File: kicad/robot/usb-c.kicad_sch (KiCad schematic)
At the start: 11 parts

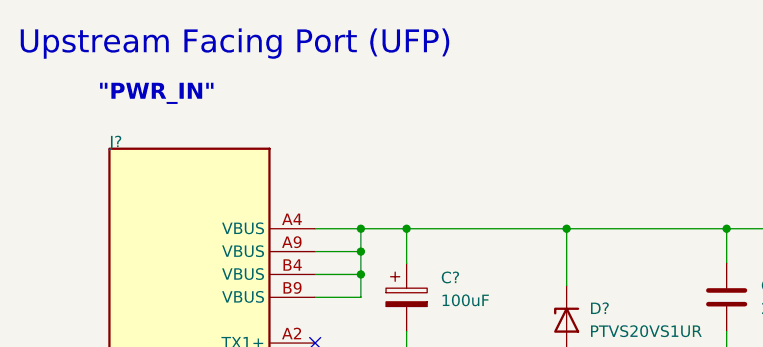
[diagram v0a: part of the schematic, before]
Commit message: Removed some outdated text
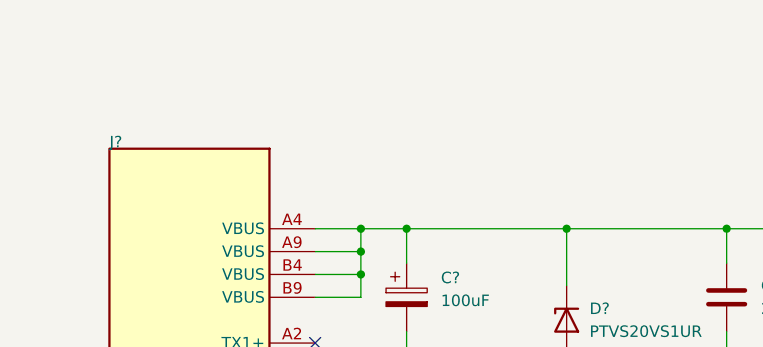
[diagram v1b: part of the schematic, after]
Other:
- note removed: ""PWR_IN""
- note removed: "Upstream Facing Port (UFP)"
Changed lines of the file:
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@@
     (stroke (width 0.254) (type default) (color 0 0 0 0))
-  )
-  (text "\"PWR_IN\"" (at 115.57 57.15 180)
-    (effects (font (size 1.778 1.778) bold) (justify left bottom))
-  )
-  (text "Upstream Facing Port (UFP)" (at 106.68 52.07 180)
-    (effects (font (size 2.54 2.54)) (justify left bottom))
   )
   (label "D-" (at 139.7 116.84 0)

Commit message: Automated annotation for full project
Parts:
- gave numbers to parts that had none: 11
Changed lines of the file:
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@@
   (symbol (lib_id "Device:C") (at 185.42 78.74 0) (unit 1)
     (in_bom yes) (on_board yes) (fields_autoplaced)
-    (property "Reference" "C?" (id 0) (at 189.23 77.4699 0)
+    (property "Reference" "C20" (id 0) (at 189.23 77.4699 0)
       (effects (font (size 1.27 1.27)) (justify left))
     )
@@
   (symbol (lib_id "Connector:TestPoint") (at 157.48 124.46 270) (unit 1)
     (in_bom yes) (on_board yes)
-    (property "Reference" "TP?" (id 0) (at 162.56 121.92 90)
+    (property "Reference" "TP8" (id 0) (at 162.56 121.92 90)
       (effects (font (size 1.27 1.27)) (justify left))
     )
@@
   (symbol (lib_id "Device:D_Zener") (at 167.64 81.28 90) (mirror x) (unit 1)
     (in_bom yes) (on_board yes)
-    (property "Reference" "D?" (id 0) (at 170.18 80.0099 90)
+    (property "Reference" "D2" (id 0) (at 170.18 80.0099 90)
       (effects (font (size 1.27 1.27)) (justify right))
     )
@@
   (symbol (lib_id "Device:C_Polarized") (at 149.86 78.74 0) (unit 1)
     (in_bom yes) (on_board yes) (fields_autoplaced)
-    (property "Reference" "C?" (id 0) (at 153.67 76.5809 0)
+    (property "Reference" "C4" (id 0) (at 153.67 76.5809 0)
       (effects (font (size 1.27 1.27)) (justify left))
     )
@@
   (symbol (lib_id "Connector:TestPoint") (at 175.26 129.54 0) (unit 1)
     (in_bom yes) (on_board yes)
-    (property "Reference" "TP?" (id 0) (at 177.8 124.46 0)
+    (property "Reference" "TP9" (id 0) (at 177.8 124.46 0)
       (effects (font (size 1.27 1.27)) (justify left))
     )
@@
   (symbol (lib_id "Device:C") (at 170.18 142.24 0) (unit 1)
     (in_bom yes) (on_board yes) (fields_autoplaced)
-    (property "Reference" "C?" (id 0) (at 173.99 140.9699 0)
+    (property "Reference" "C19" (id 0) (at 173.99 140.9699 0)
       (effects (font (size 1.27 1.27)) (justify left))
     )
@@
   (symbol (lib_id "Connector:TestPoint") (at 193.04 71.12 0) (unit 1)
     (in_bom yes) (on_board yes)
-    (property "Reference" "TP?" (id 0) (at 195.58 66.04 0)
+    (property "Reference" "TP11" (id 0) (at 195.58 66.04 0)
       (effects (font (size 1.27 1.27)) (justify left))
     )
@@
   (symbol (lib_id "Top-altium-import:0_mirrored_USBC_Receptacle_SMD_RA") (at 134.62 62.23 0) (unit 1)
     (in_bom yes) (on_board yes)
-    (property "Reference" "J?" (id 0) (at 116.84 62.23 0)
+    (property "Reference" "J1" (id 0) (at 116.84 62.23 0)
       (effects (font (size 1.27 1.27)) (justify left bottom))
     )
@@
   (symbol (lib_id "Connector:TestPoint") (at 147.32 121.92 270) (unit 1)
     (in_bom yes) (on_board yes) (fields_autoplaced)
-    (property "Reference" "TP?" (id 0) (at 152.4 120.6499 90)
+    (property "Reference" "TP7" (id 0) (at 152.4 120.6499 90)
       (effects (font (size 1.27 1.27)) (justify left))
     )
@@
   (symbol (lib_id "Connector:TestPoint") (at 175.26 132.08 180) (unit 1)
     (in_bom yes) (on_board yes)
-    (property "Reference" "TP?" (id 0) (at 177.8 134.62 0)
+    (property "Reference" "TP10" (id 0) (at 177.8 134.62 0)
       (effects (font (size 1.27 1.27)) (justify right))
     )
@@
   (symbol (lib_id "Device:C") (at 157.48 142.24 0) (unit 1)
     (in_bom yes) (on_board yes)
-    (property "Reference" "C?" (id 0) (at 160.782 140.97 0)
-      (effects (font (size 1.27 1.27)) (justify left))
-    )
+    (property "Reference" "C18" (id 0) (at 160.782 140.97 0)
+      (effects (font (size 1.27 1.27)) (justify left))
+    )

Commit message: Moved USB-C symbol to connector lib
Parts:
- J1: symbol Top-altium-import:0_mirrored_USBC_Receptacle_SMD_RA -> Connector:0_mirrored_USBC_Receptacle_SMD_RA
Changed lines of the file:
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@@
     (pin "1")
   )
-  (symbol (lib_id "Top-altium-import:0_mirrored_USBC_Receptacle_SMD_RA") (at 134.62 62.23 0) (unit 1)
+  (symbol (lib_id "Connector:0_mirrored_USBC_Receptacle_SMD_RA") (at 134.62 62.23 0) (unit 1)
     (in_bom yes) (on_board yes)
     (property "Reference" "J1" (id 0) (at 116.84 62.23 0)

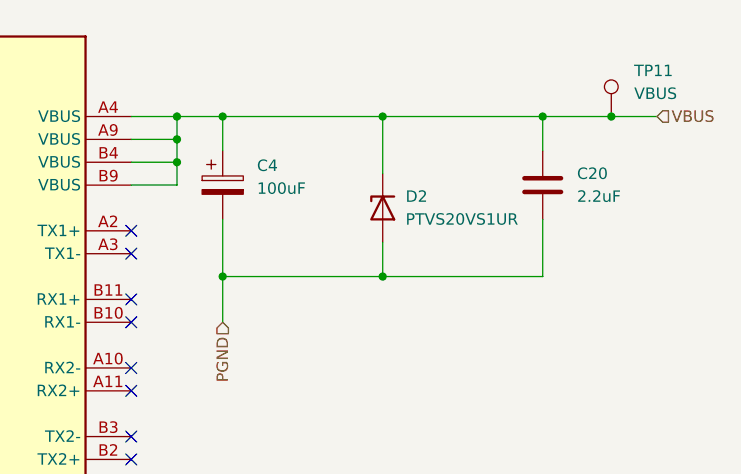
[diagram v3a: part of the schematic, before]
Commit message: Assigned capacitor footprints
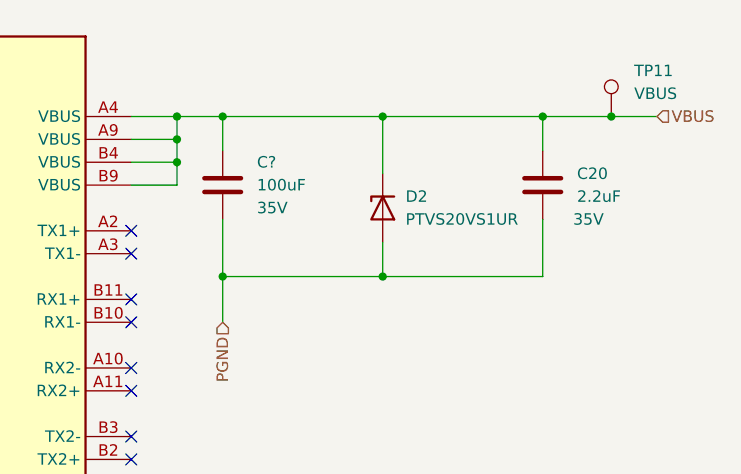
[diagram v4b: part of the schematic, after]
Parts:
- removed C4: 100uF, symbol Device:C_Polarized
- added C?: 100uF, Capacitor_SMD:C_1210_3225Metric, symbol Device:C
- C18, C19: footprint (none) -> Capacitor_SMD:C_0402_1005Metric
- C20: footprint (none) -> Capacitor_SMD:C_0805_2012Metric
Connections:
- net PGND: now also C?.2
- net VBUS: now also C?.1
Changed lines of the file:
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@@
   )
   (symbol (lib_id "Device:C") (at 185.42 78.74 0) (unit 1)
+    (in_bom yes) (on_board yes)
+    (property "Reference" "C20" (id 0) (at 189.23 77.4699 0)
+      (effects (font (size 1.27 1.27)) (justify left))
+    )
+    (property "Value" "2.2uF" (id 1) (at 189.23 80.0099 0)
+      (effects (font (size 1.27 1.27)) (justify left))
+    )
+    (property "Footprint" "Capacitor_SMD:C_0805_2012Metric" (id 2) (at 186.3852 82.55 0)
+      (effects (font (size 1.27 1.27)) hide)
+    )
+    (property "Datasheet" "~" (id 3) (at 185.42 78.74 0)
+      (effects (font (size 1.27 1.27)) hide)
+    )
+    (property "Description" "35V" (id 4) (at 190.5 82.55 0))
+    (pin "1")
+    (pin "2")
+  )
+  (symbol (lib_id "Connector:TestPoint") (at 157.48 124.46 270) (unit 1)
+    (in_bom yes) (on_board yes)
+    (property "Reference" "TP8" (id 0) (at 162.56 121.92 90)
+      (effects (font (size 1.27 1.27)) (justify left))
+    )
+    (property "Value" "D+" (id 1) (at 162.56 124.46 90)
+      (effects (font (size 1.27 1.27)) (justify left))
+    )
+    (property "Footprint" "" (id 2) (at 157.48 129.54 0)
+      (effects (font (size 1.27 1.27)) hide)
+    )
+    (property "Datasheet" "~" (id 3) (at 157.48 129.54 0)
+      (effects (font (size 1.27 1.27)) hide)
+    )
+    (pin "1")
+  )
+  (symbol (lib_id "Device:D_Zener") (at 167.64 81.28 90) (mirror x) (unit 1)
+    (in_bom yes) (on_board yes)
+    (property "Reference" "D2" (id 0) (at 170.18 80.0099 90)
+      (effects (font (size 1.27 1.27)) (justify right))
+    )
+    (property "Value" "PTVS20VS1UR" (id 1) (at 170.18 82.5499 90)
+      (effects (font (size 1.27 1.27)) (justify right))
+    )
+    (property "Footprint" "" (id 2) (at 167.64 81.28 0)
+      (effects (font (size 1.27 1.27)) hide)
+    )
+    (property "Datasheet" "~" (id 3) (at 167.64 81.28 0)
+      (effects (font (size 1.27 1.27)) hide)
+    )
+    (pin "1")
+    (pin "2")
+  )
+  (symbol (lib_id "Device:C") (at 149.86 78.74 0) (unit 1)
     (in_bom yes) (on_board yes) (fields_autoplaced)
-    (property "Reference" "C20" (id 0) (at 189.23 77.4699 0)
-      (effects (font (size 1.27 1.27)) (justify left))
-    )
-    (property "Value" "2.2uF" (id 1) (at 189.23 80.0099 0)
-      (effects (font (size 1.27 1.27)) (justify left))
-    )
-    (property "Footprint" "" (id 2) (at 186.3852 82.55 0)
-      (effects (font (size 1.27 1.27)) hide)
-    )
-    (property "Datasheet" "~" (id 3) (at 185.42 78.74 0)
-      (effects (font (size 1.27 1.27)) hide)
-    )
-    (pin "1")
-    (pin "2")
-  )
-  (symbol (lib_id "Connector:TestPoint") (at 157.48 124.46 270) (unit 1)
-    (in_bom yes) (on_board yes)
-    (property "Reference" "TP8" (id 0) (at 162.56 121.92 90)
-      (effects (font (size 1.27 1.27)) (justify left))
-    )
-    (property "Value" "D+" (id 1) (at 162.56 124.46 90)
-      (effects (font (size 1.27 1.27)) (justify left))
-    )
-    (property "Footprint" "" (id 2) (at 157.48 129.54 0)
-      (effects (font (size 1.27 1.27)) hide)
-    )
-    (property "Datasheet" "~" (id 3) (at 157.48 129.54 0)
-      (effects (font (size 1.27 1.27)) hide)
-    )
-    (pin "1")
-  )
-  (symbol (lib_id "Device:D_Zener") (at 167.64 81.28 90) (mirror x) (unit 1)
-    (in_bom yes) (on_board yes)
-    (property "Reference" "D2" (id 0) (at 170.18 80.0099 90)
-      (effects (font (size 1.27 1.27)) (justify right))
-    )
-    (property "Value" "PTVS20VS1UR" (id 1) (at 170.18 82.5499 90)
-      (effects (font (size 1.27 1.27)) (justify right))
-    )
-    (property "Footprint" "" (id 2) (at 167.64 81.28 0)
-      (effects (font (size 1.27 1.27)) hide)
-    )
-    (property "Datasheet" "~" (id 3) (at 167.64 81.28 0)
-      (effects (font (size 1.27 1.27)) hide)
-    )
-    (pin "1")
-    (pin "2")
-  )
-  (symbol (lib_id "Device:C_Polarized") (at 149.86 78.74 0) (unit 1)
-    (in_bom yes) (on_board yes) (fields_autoplaced)
-    (property "Reference" "C4" (id 0) (at 153.67 76.5809 0)
-      (effects (font (size 1.27 1.27)) (justify left))
-    )
-    (property "Value" "100uF" (id 1) (at 153.67 79.1209 0)
-      (effects (font (size 1.27 1.27)) (justify left))
-    )
-    (property "Footprint" "" (id 2) (at 150.8252 82.55 0)
+    (property "Reference" "C?" (id 0) (at 153.67 76.1999 0)
+      (effects (font (size 1.27 1.27)) (justify left))
+    )
+    (property "Value" "100uF" (id 1) (at 153.67 78.7399 0)
+      (effects (font (size 1.27 1.27)) (justify left))
+    )
+    (property "Footprint" "Capacitor_SMD:C_1210_3225Metric" (id 2) (at 150.8252 82.55 0)
       (effects (font (size 1.27 1.27)) hide)
     )
     (property "Datasheet" "~" (id 3) (at 149.86 78.74 0)
       (effects (font (size 1.27 1.27)) hide)
+    )
+    (property "Description" "35V" (id 4) (at 153.67 81.2799 0)
+      (effects (font (size 1.27 1.27)) (justify left))
     )
     (pin "1")
@@
       (effects (font (size 1.27 1.27)) (justify left))
     )
-    (property "Footprint" "" (id 2) (at 171.1452 146.05 0)
+    (property "Footprint" "Capacitor_SMD:C_0402_1005Metric" (id 2) (at 171.1452 146.05 0)
       (effects (font (size 1.27 1.27)) hide)
     )
@@
       (effects (font (size 1.27 1.27)) (justify left))
     )
-    (property "Footprint" "" (id 2) (at 158.4452 146.05 0)
-      (effects (font (size 1.27 1.27)) hide)
-    )
+    (property "Footprint" "Capacitor_SMD:C_0402_1005Metric" (id 2) (at 158.4452 146.05 0)
+      (effects (font (size 1.27 1.27)) hide)
+    )

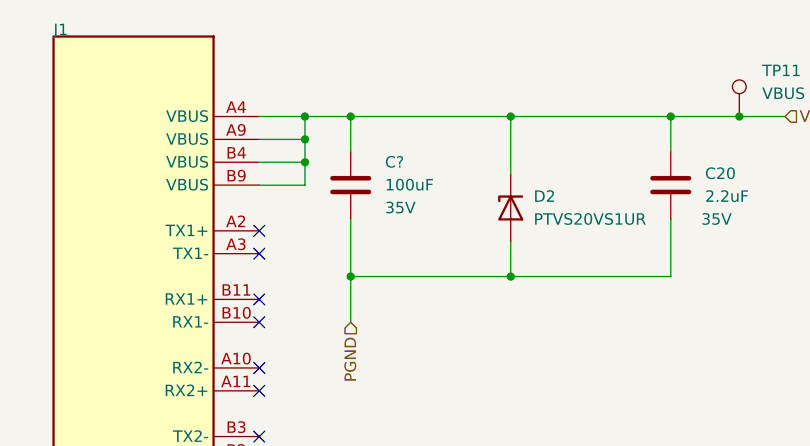
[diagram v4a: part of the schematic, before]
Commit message: Added missing annotations
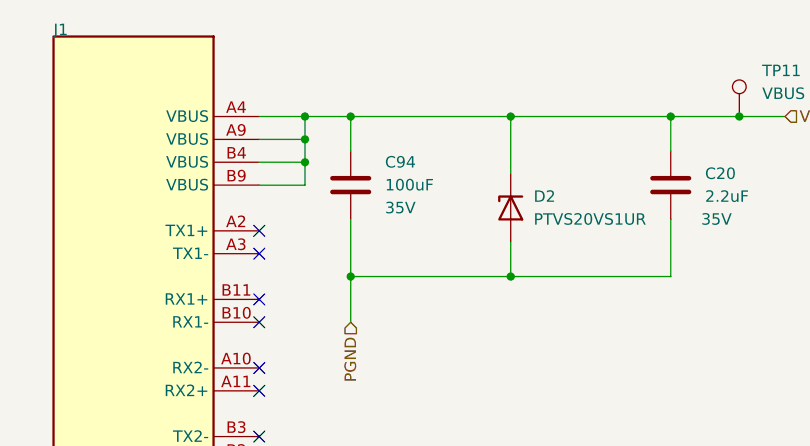
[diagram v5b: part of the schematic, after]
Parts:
- gave numbers to parts that had none: 1
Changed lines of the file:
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@@
   (symbol (lib_id "Device:C") (at 149.86 78.74 0) (unit 1)
     (in_bom yes) (on_board yes) (fields_autoplaced)
-    (property "Reference" "C?" (id 0) (at 153.67 76.1999 0)
+    (property "Reference" "C94" (id 0) (at 153.67 76.1999 0)
       (effects (font (size 1.27 1.27)) (justify left))
     )

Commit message: Adding footprint and model to Nexperia_CFP3_SOD-123W
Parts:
- D2: footprint (none) -> Diode_SMD:Nexperia_CFP3_SOD-123W; Part Number (none) -> PTVS20VS1UR
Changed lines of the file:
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@@
       (effects (font (size 1.27 1.27)) (justify right))
     )
-    (property "Footprint" "" (id 2) (at 167.64 81.28 0)
+    (property "Footprint" "Diode_SMD:Nexperia_CFP3_SOD-123W" (id 2) (at 167.64 81.28 0)
       (effects (font (size 1.27 1.27)) hide)
     )
-    (property "Datasheet" "~" (id 3) (at 167.64 81.28 0)
+    (property "Datasheet" "https://www.mouser.jp/datasheet/2/916/PTVSXS1UR_SER-1545507.pdf" (id 3) (at 167.64 81.28 0)
       (effects (font (size 1.27 1.27)) hide)
     )
+    (property "Part Number" "PTVS20VS1UR" (id 4) (at 167.64 81.28 0)
+      (effects (font (size 1.27 1.27)) hide)
+    )
+    (property "Description" "TVS Diode 20V" (id 5) (at 167.64 81.28 0)
+      (effects (font (size 1.27 1.27)) hide)
+    )

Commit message: Added footprint to remaining test points
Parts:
- TP10, TP11, TP7, TP8, TP9: footprint (none) -> TestPoint:KEYSTONE_5002
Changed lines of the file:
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@@
       (effects (font (size 1.27 1.27)) (justify left))
     )
-    (property "Footprint" "" (id 2) (at 157.48 129.54 0)
+    (property "Footprint" "TestPoint:KEYSTONE_5002" (id 2) (at 157.48 129.54 0)
       (effects (font (size 1.27 1.27)) hide)
     )
@@
       (effects (font (size 1.27 1.27)) (justify left))
     )
-    (property "Footprint" "" (id 2) (at 180.34 129.54 0)
+    (property "Footprint" "TestPoint:KEYSTONE_5002" (id 2) (at 180.34 129.54 0)
       (effects (font (size 1.27 1.27)) hide)
     )
@@
       (effects (font (size 1.27 1.27)) (justify left))
     )
-    (property "Footprint" "" (id 2) (at 198.12 71.12 0)
+    (property "Footprint" "TestPoint:KEYSTONE_5002" (id 2) (at 198.12 71.12 0)
       (effects (font (size 1.27 1.27)) hide)
     )
@@
       (effects (font (size 1.27 1.27)) (justify left))
     )
-    (property "Footprint" "" (id 2) (at 147.32 127 0)
+    (property "Footprint" "TestPoint:KEYSTONE_5002" (id 2) (at 147.32 127 0)
       (effects (font (size 1.27 1.27)) hide)
     )
@@
       (effects (font (size 1.27 1.27)) (justify right))
     )
-    (property "Footprint" "" (id 2) (at 170.18 132.08 0)
-      (effects (font (size 1.27 1.27)) hide)
-    )
+    (property "Footprint" "TestPoint:KEYSTONE_5002" (id 2) (at 170.18 132.08 0)
+      (effects (font (size 1.27 1.27)) hide)
+    )
